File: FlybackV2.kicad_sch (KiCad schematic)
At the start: 73 parts, among them J2 Divisor, J3 Conn_01x03, J4 Coils, Q6 2N3906, T2 0399-T208, U1 LT8304, U9 MAX4239

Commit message: finish the route, in revision
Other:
- moved on the sheet: C19, C20, C3, C4, C42, C5, D14, D26, H1, H2, H3, H4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

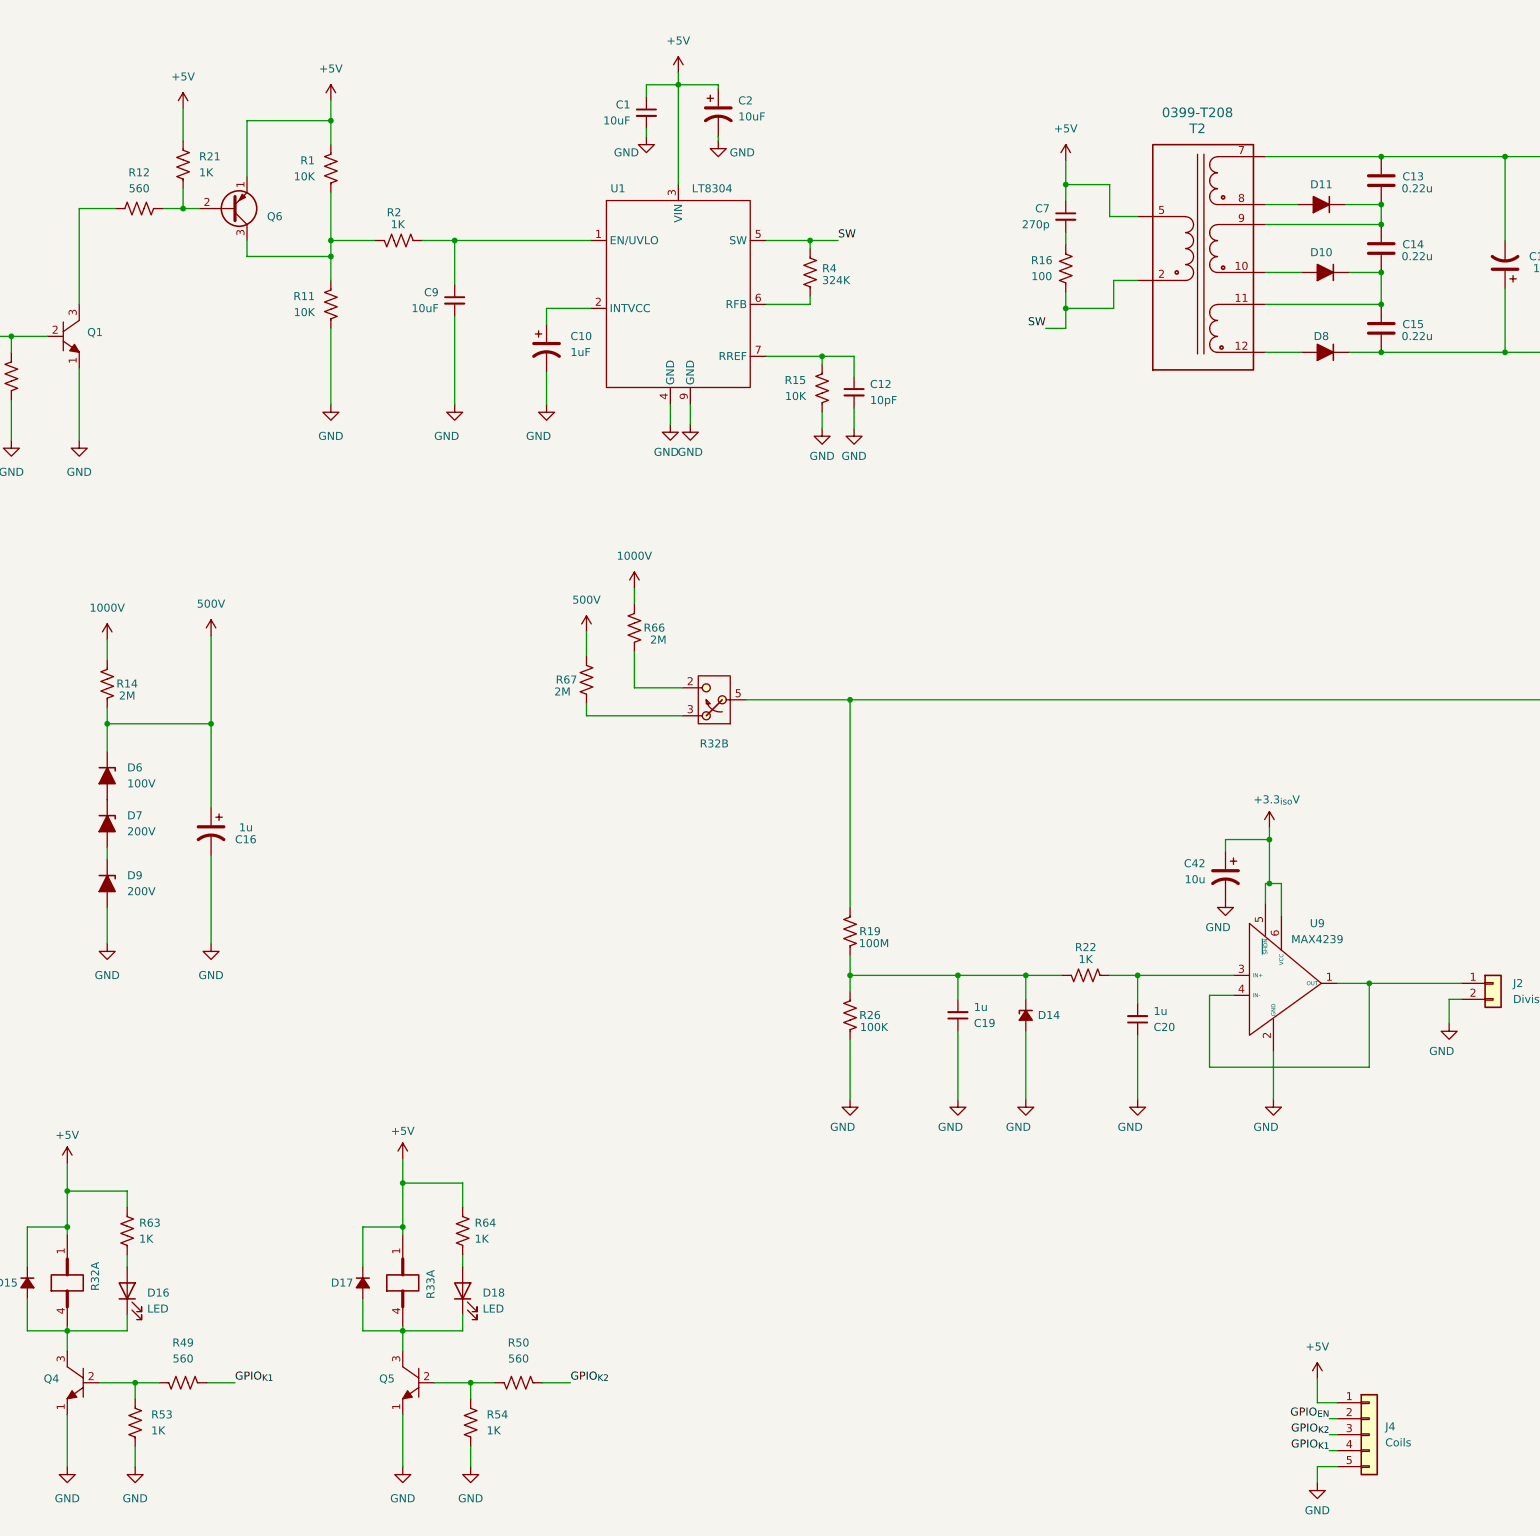
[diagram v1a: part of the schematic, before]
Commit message: now has a C for the 12V source
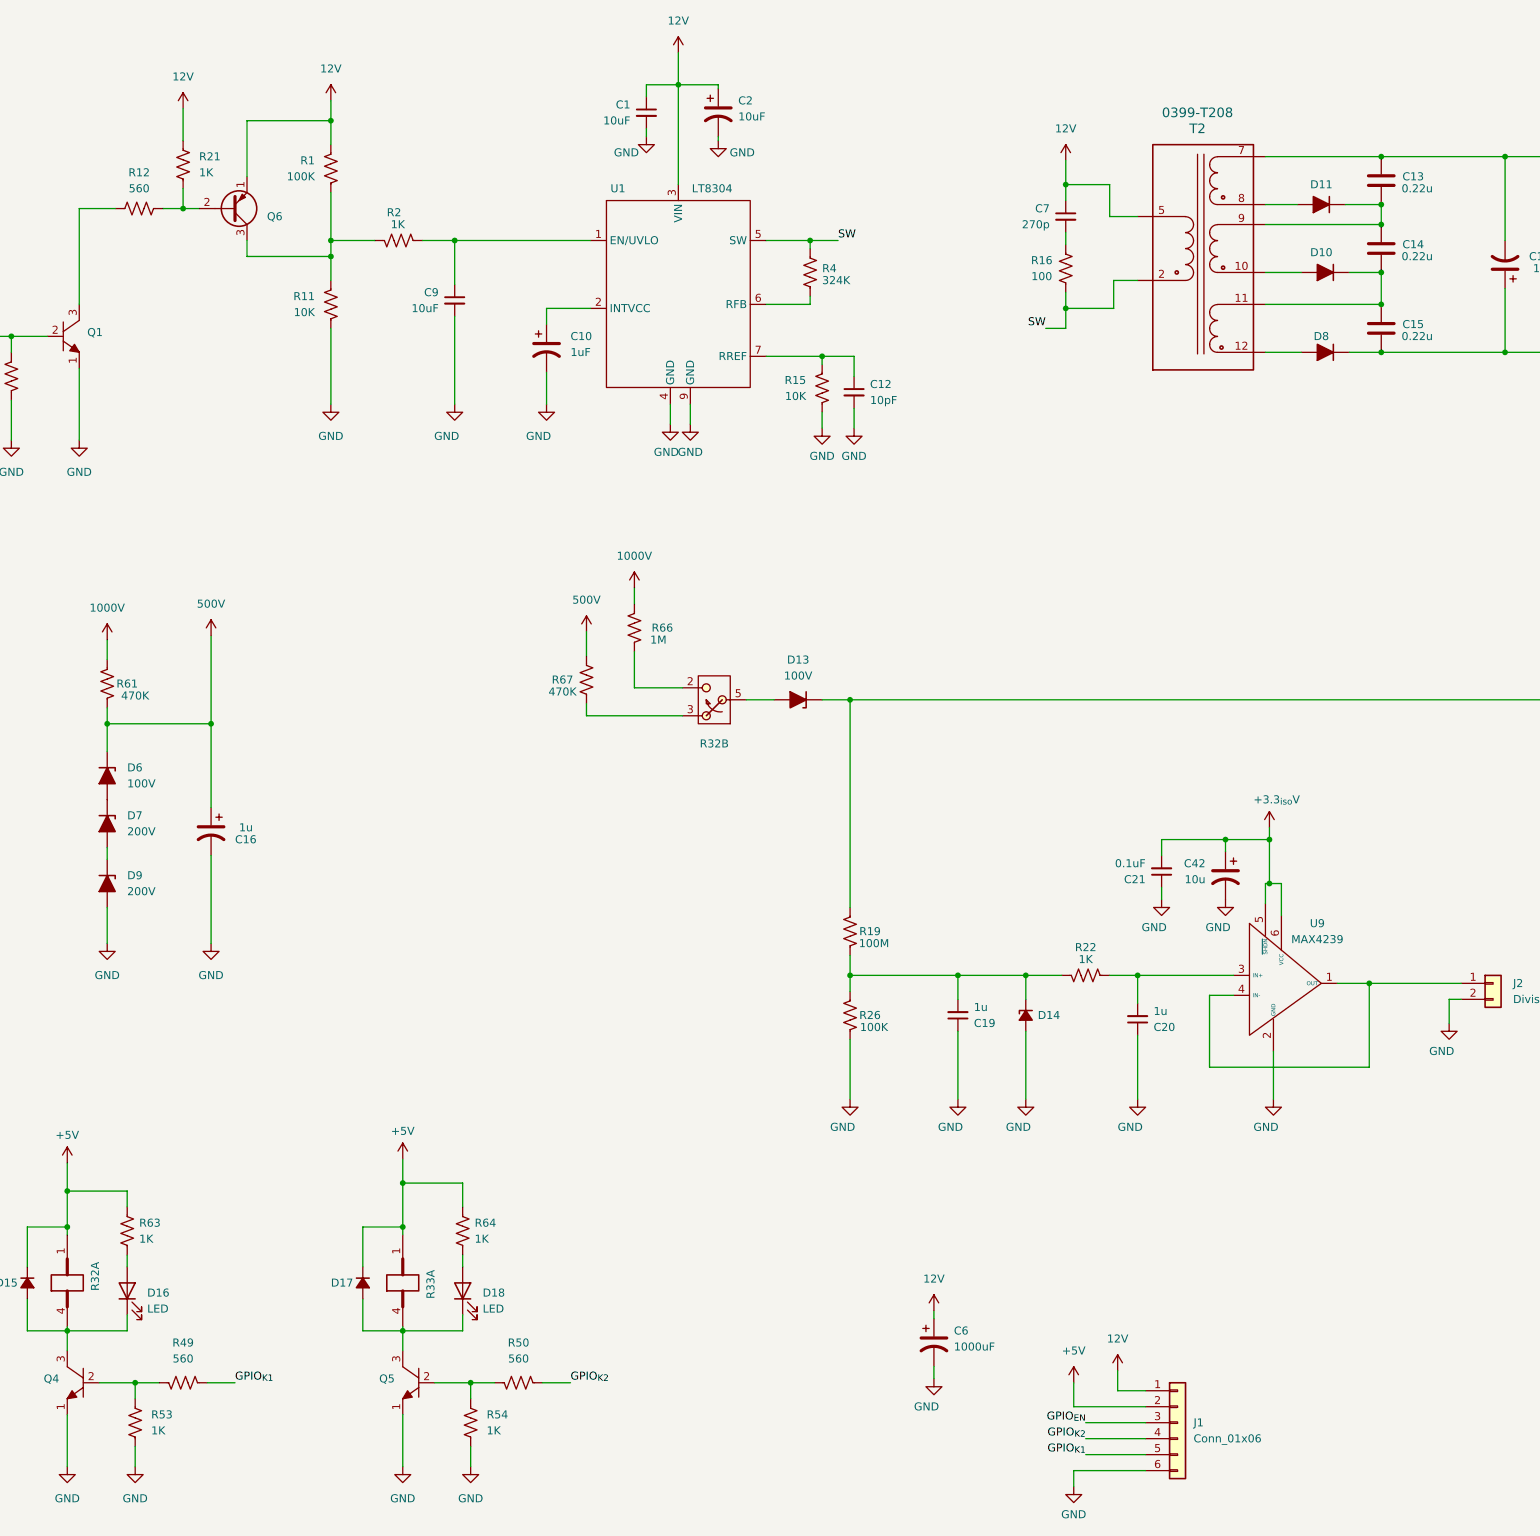
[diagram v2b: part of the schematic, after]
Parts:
- removed J4: Coils, Connector_PinHeader_2.54mm:PinHeader_1x05_P2.54mm_Vertical, symbol Connector_Generic:Conn_01x05
- removed R14: 2M, Resistor_THT:R_Axial_DIN0207_L6.3mm_D2.5mm_P10.16mm_Horizontal, symbol Device:R_US
- added C21: 0.1uF, Capacitor_SMD:C_0805_2012Metric, symbol Device:C_Small
- added C6: 1000uF, Capacitor_THT:CP_Radial_D10.0mm_P5.00mm, symbol Device:C_Polarized_US
- added D13: 100V, Diode_THT:D_A-405_P5.08mm_Vertical_KathodeUp, symbol Device:D_Zener_Filled
- added J1: Conn_01x06, Connector_PinSocket_2.54mm:PinSocket_1x06_P2.54mm_Vertical, symbol Connector_Generic:Conn_01x06
- added R61: 470K, Resistor_THT:R_Axial_DIN0207_L6.3mm_D2.5mm_P15.24mm_Horizontal, symbol Device:R_US
- C13, C14, C15: LCSC Part (none) -> C76694
- H1, H2, H3, H4: now in the parts list
- R1: value 10K -> 100K
- R66: value 2M -> 1M
- R67: value 2M -> 470K
- U1: LCSC Part C580283 -> C673691
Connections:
- net +3.3_{iso}V: now also C21.2
- net +5V: now also J1.2 (Pin_2); no longer C1.1, C2.1, C7.1, Q6.1 (E), R1.1, R21.1, T2.5, U1.3 (VIN)
- net 1000V: now also R61.2
- net 500V: now also R61.1
- net GND: now also C21.1, C6.2, J1.6 (Pin_6)
- net GPIO_{EN}: now also J1.3 (Pin_3)
- net GPIO_{K1}: now also J1.5 (Pin_5)
- net GPIO_{K2}: now also J1.4 (Pin_4)
- net at R19.2, R33.2: now also D13.1 (K); no longer R32.5
- new net: D13.2 (A), R32.5
- new net 12V: C1.1, C2.1, C6.1, C7.1, J1.1 (Pin_1), Q6.1 (E), R1.1, R21.1, T2.5, U1.3 (VIN)

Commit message: update: it versin goes to production
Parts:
- C13, C14, C15: value 0.22u -> 0.22uF
- C16, C17, C19, C20: value 1u -> 1uF
- C3: value 0.1u -> 0.1uF
- C4, C42, C5: value 10u -> 10uF
- C6: footprint Capacitor_THT:CP_Radial_D10.0mm_P5.00mm -> Capacitor_THT:CP_Radial_D13.0mm_P5.00mm
- J1: footprint Connector_PinSocket_2.54mm:PinSocket_1x06_P2.54mm_Vertical -> Connector_PinHeader_2.54mm:PinHeader_1x06_P2.54mm_Vertical
- Q6: LCSC Part (none) -> C9809
- R11: value 10K -> 1K
- R2: value 1K -> 0
- R26: footprint Resistor_THT:R_Axial_DIN0309_L9.0mm_D3.2mm_P20.32mm_Horizontal -> Resistor_THT:R_Axial_DIN0207_L6.3mm_D2.5mm_P15.24mm_Horizontal
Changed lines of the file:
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@@
 			)
 		)
-		(property "Value" "10u"
+		(property "Value" "10uF"
 			(at 378.46 62.2362 0)
 			(effects
@@
 			)
 		)
-		(property "Footprint" "Resistor_THT:R_Axial_DIN0309_L9.0mm_D3.2mm_P20.32mm_Horizontal"
+		(property "Footprint" "Resistor_THT:R_Axial_DIN0207_L6.3mm_D2.5mm_P15.24mm_Horizontal"
 			(at 190.246 184.531 90)
 			(effects
@@
 			)
 		)
-		(property "Footprint" "Connector_PinSocket_2.54mm:PinSocket_1x06_P2.54mm_Vertical"
+		(property "Footprint" "Connector_PinHeader_2.54mm:PinHeader_1x06_P2.54mm_Vertical"
 			(at 241.3 249.555 0)
 			(effects
@@
 			)
 		)
-		(property "Value" "0.1u"
+		(property "Value" "0.1uF"
 			(at 387.985 62.2362 0)
 			(effects
@@
 			)
 		)
-		(property "Value" "10u"
+		(property "Value" "10uF"
 			(at 245.745 163.1949 0)
 			(effects
@@
 			)
 		)
-		(property "Value" "0.22u"
+		(property "Value" "0.22uF"
 			(at 279.4 53.34 0)
 			(effects
@@
 			)
 		)
-		(property "Value" "0.22u"
+		(property "Value" "0.22uF"
 			(at 279.4 76.835 0)
 			(effects
@@
 			)
 		)
-		(property "Value" "0.22u"
+		(property "Value" "0.22uF"
 			(at 279.4 64.135 0)
 			(effects
@@
 			)
 		)
-		(property "Value" "10u"
+		(property "Value" "10uF"
 			(at 343.535 60.9662 0)
 			(effects
@@
 			)
 		)
-		(property "Value" "10K"
+		(property "Value" "1K"
 			(at 104.14 73.0249 0)
 			(effects
@@
 			)
 		)
-		(property "Value" "1u"
+		(property "Value" "1uF"
 			(at 297.815 66.04 0)
 			(effects
@@
 			)
 		)
-		(property "Footprint" "Capacitor_THT:CP_Radial_D10.0mm_P5.00mm"
+		(property "Footprint" "Capacitor_THT:CP_Radial_D13.0mm_P5.00mm"
 			(at 202.565 236.855 0)
 			(effects
@@
 			)
 		)
-		(property "Value" "1K"
+		(property "Value" "0"
 			(at 116.2051 59.055 90)
 			(effects
@@
 			)
 		)
+		(property "LCSC Part" "C9809"
+			(at 90.805 56.515 0)
+			(effects
+				(font
+					(size 1.27 1.27)
+				)
+				(hide yes)
+			)
+		)
 		(pin "3"
 		)
@@
 			)
 		)
-		(property "Value" "1u"
+		(property "Value" "1uF"
 			(at 92.075 154.94 0)
 			(effects
@@
 			)
 		)
-		(property "Value" "1u"
+		(property "Value" "1uF"
 			(at 237.49 184.1438 0)
 			(effects
@@
 			)
 		)
-		(property "Value" "1u"
+		(property "Value" "1uF"
 			(at 208.915 183.5088 0)
 			(effects

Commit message: update: order in the schematic
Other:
- note added: "0399-T208 Transformer 1000V"
- note added: "500V zeners"
- note added: "AMS1117-3.3"
- note added: "BJT Coils"
- note added: "Coils connectors"
- note added: "LT8304"
- note added: "M3 Screws"
- note added: "Relay 1000v and 500v"
- moved on the sheet: C1, C10, C12, C13, C14, C15, C16, C17, C19, C2, C20, C21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

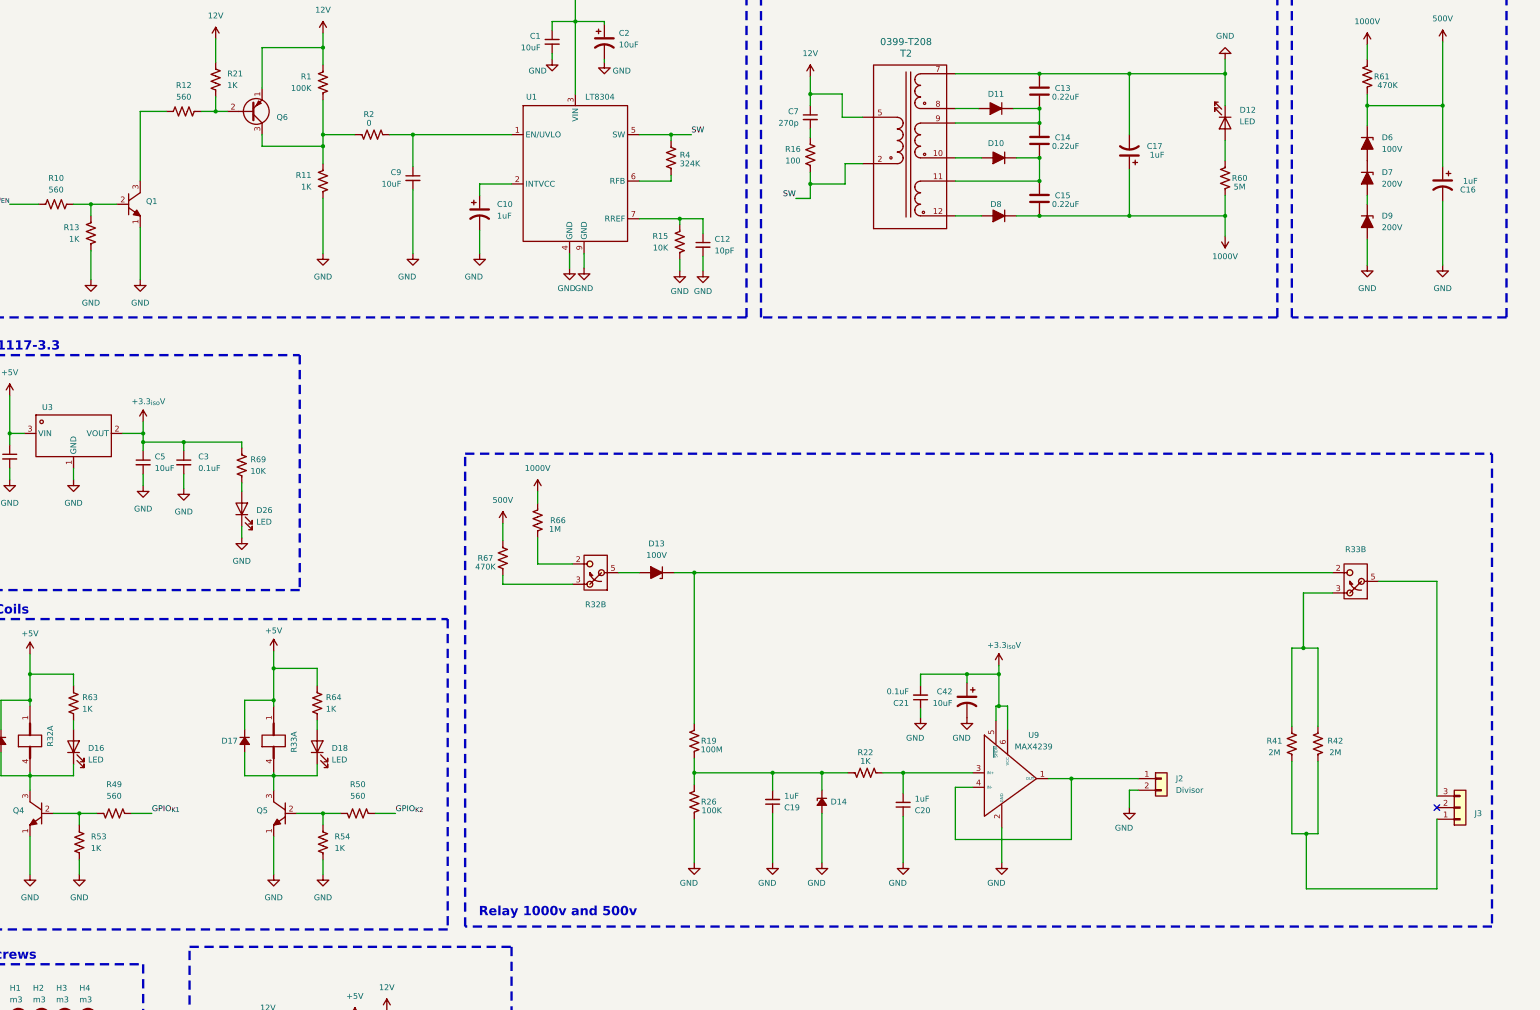
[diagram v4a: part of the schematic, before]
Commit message: uptade: jlcs part number
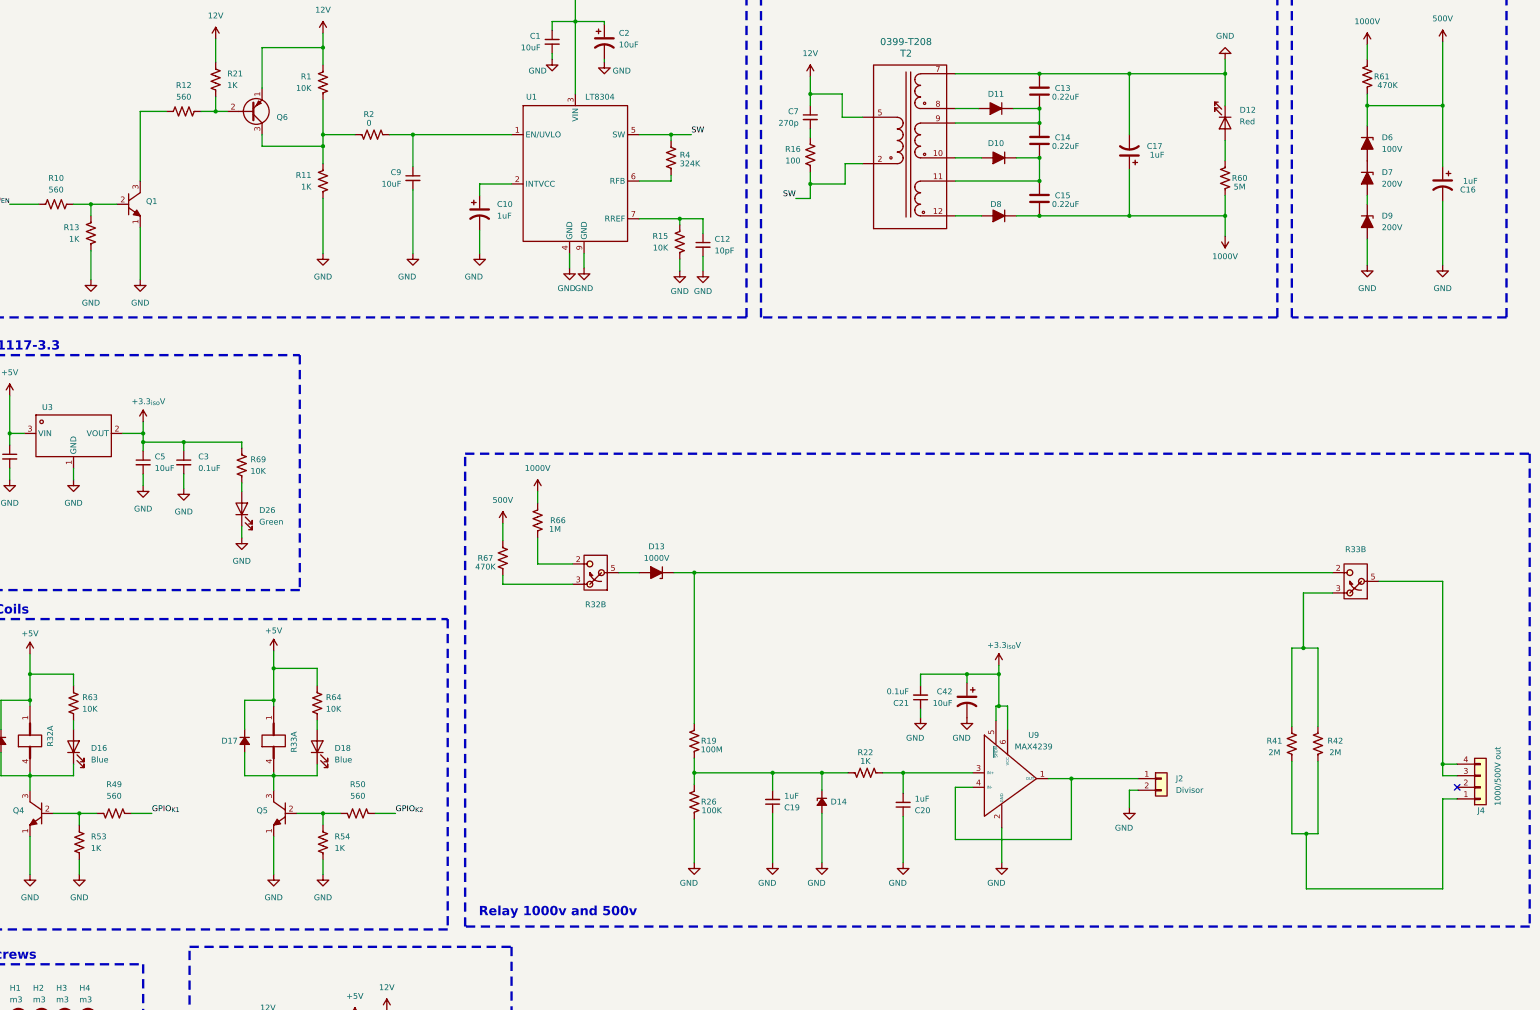
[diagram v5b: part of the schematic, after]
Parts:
- removed J3: Conn_01x03, TerminalBlock_Phoenix:TerminalBlock_Phoenix_MKDS-1,5-3-5.08_1x03_P5.08mm_Horizontal, symbol Connector_Generic:Conn_01x03
- added J4: 1000/500V out, TerminalBlock_Phoenix:TerminalBlock_Phoenix_MKDS-1,5-4-5.08_1x04_P5.08mm_Horizontal, symbol Connector_Generic:Conn_01x04
- C1, C2, C4, C42, C5, C9: LCSC Part (none) -> C15850
- C10, C19, C20: LCSC Part (none) -> C28323
- C12: LCSC Part (none) -> C157608
- C13, C14, C15: LCSC Part C76694 -> C153037
- C21, C3: LCSC Part (none) -> C28233
- C7: LCSC Part (none) -> C113828
- D12: value LED -> Red; LCSC Part (none) -> C84256
- D13: value 100V -> 1000V
- D16, D18: value LED -> Blue; LCSC Part (none) -> C2293
- D26: value LED -> Green; LCSC Part (none) -> C2297
- R1: value 100K -> 10K; LCSC Part (none) -> C17902
- R10, R12, R49, R50: LCSC Part (none) -> C17994
- R11, R13, R21, R22, R53, R54: LCSC Part (none) -> C4410
- R15, R69: LCSC Part (none) -> C17902
- R16: LCSC Part (none) -> C17901
- R2: LCSC Part (none) -> C17888
- R4: LCSC Part (none) -> C5266167
- R63, R64: value 1K -> 10K; LCSC Part (none) -> C17902
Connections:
- net at R41.1, R42.1: now also J4.1 (Pin_1)
- net at R33.5: now also J4.3 (Pin_3), J4.4 (Pin_4)

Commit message: minor
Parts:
- R1: value 10K -> 100K; LCSC Part C17902 -> C17900
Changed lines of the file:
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@@
 			)
 		)
-		(property "Value" "10K"
+		(property "Value" "100K"
 			(at 111.76 48.2599 0)
 			(effects
@@
 			)
 		)
-		(property "LCSC Part" "C17902"
+		(property "LCSC Part" "C17900"
 			(at 114.3 46.99 0)
 			(effects
